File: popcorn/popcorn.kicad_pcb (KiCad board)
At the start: 2 copper layers, 112.4 x 88.7 mm, 56 parts, among them J1 MJ-4PP-9, J2 OLED, SW10 SW_PUSH, SW11 SW_PUSH, SW12 SW_PUSH, SW14 SW_PUSH, SW15 SW_PUSH, SW16 SW_PUSH, SW17 SW_PUSH, SW18 SW_PUSH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

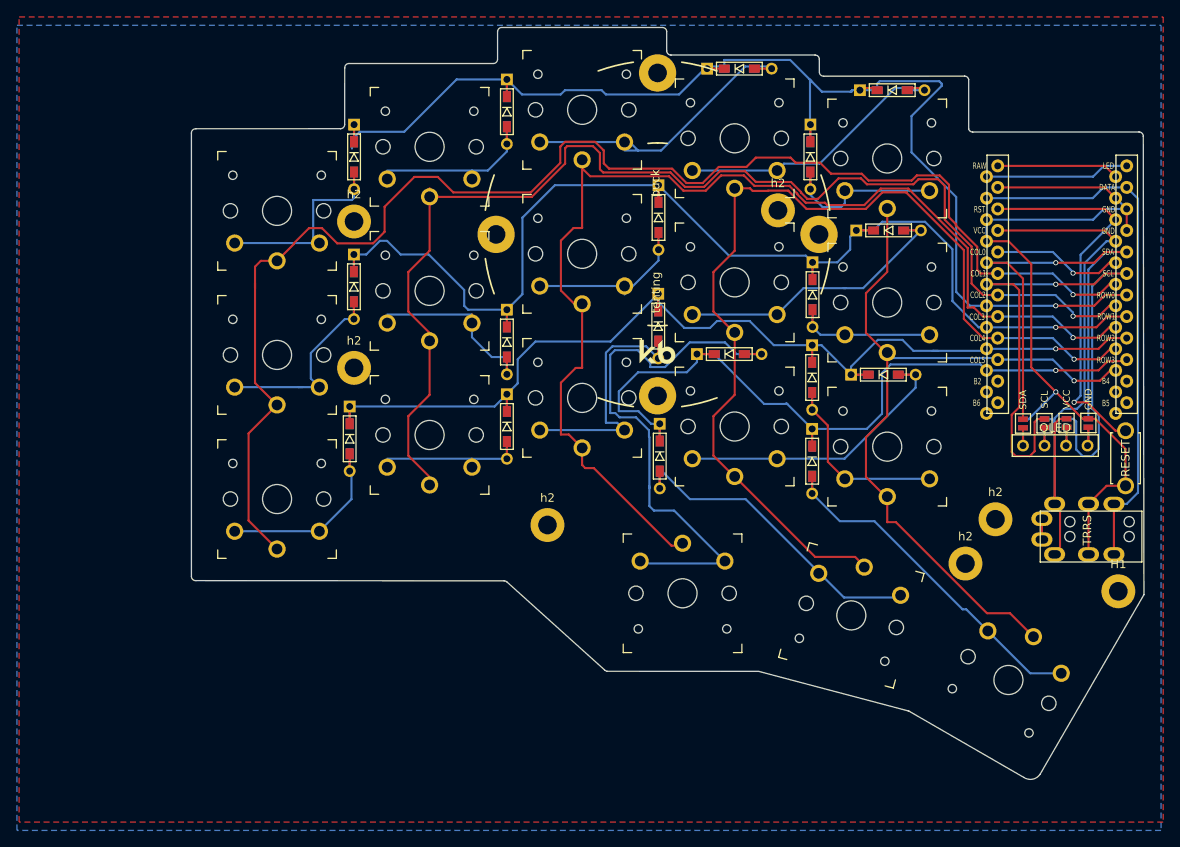
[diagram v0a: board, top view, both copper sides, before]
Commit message: Cleaned up Silkscreen
Cleaned up Silkscreen and added what it's called and who its made by. (Popcorn made by David Barr)
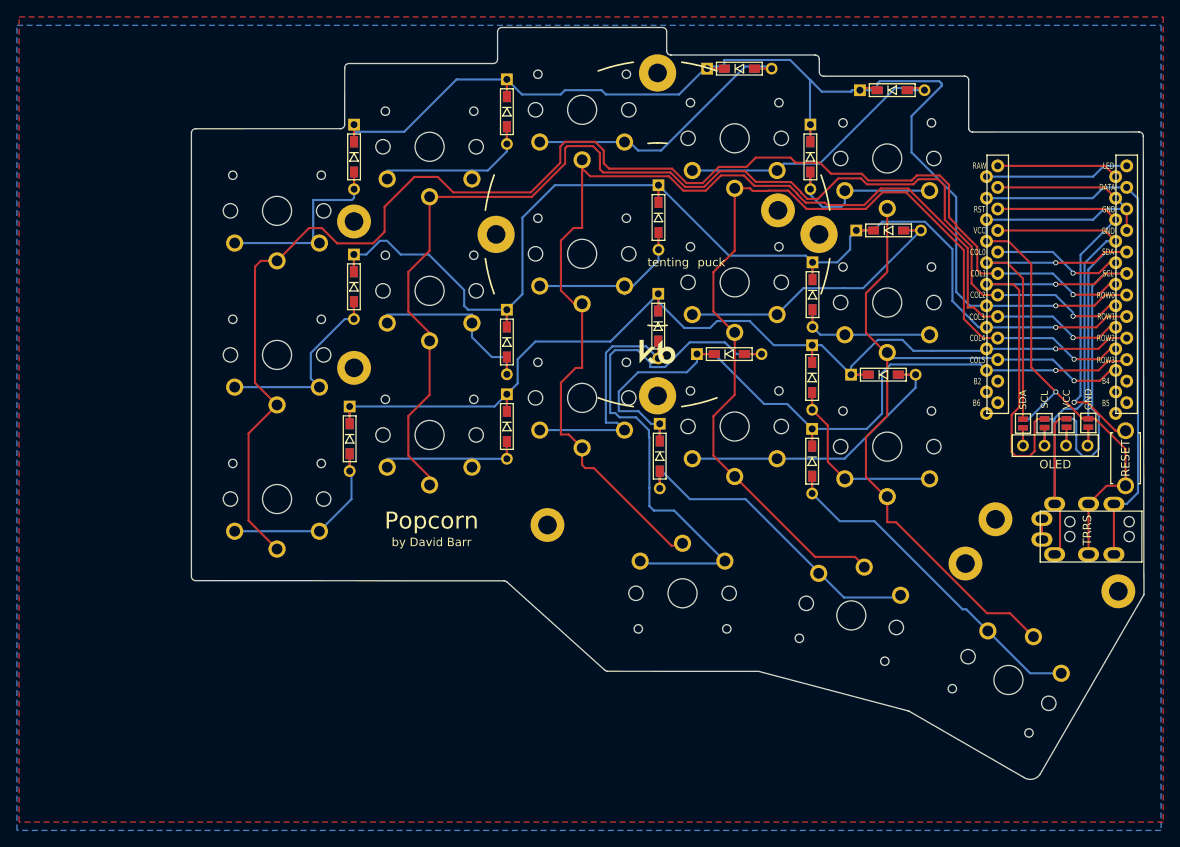
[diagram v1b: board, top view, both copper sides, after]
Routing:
- net row0: track 151.5 -> 149.9 mm
- net Net-(D4-Pad2): track 35.5 -> 33.9 mm
- net col2: track 142.1 -> 140.8 mm
- net col1: track 167.1 -> 166.5 mm
- net row2: track 128.4 -> 127.8 mm
- net Net-(D8-Pad2): track 25.8 -> 25.3 mm
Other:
- net class Default removed
- board text added: "Popcorn"
- board text added: "by David Barr"
